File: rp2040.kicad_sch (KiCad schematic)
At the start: 10 parts, among them U1 RP2040, Y1 12 MHz

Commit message: Fixing buttons / Transitioning to new computer.
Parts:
- RST1: footprint ScottoKeebs_Components:Button_MJTP1243 -> 3rd_party_footprints:SW4_PTS815 SJM 250 SMTR LFS_CNK
- renumbered C1 to C10, C3 to C11, C6 to C12, C8 to C7, C7 to C8, C2 to C9, U1 to U3
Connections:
- no-connect marks 4 -> 24
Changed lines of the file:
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@@
+	)
+	(no_connect
+		(at 105.41 119.38)
+	)
+	(no_connect
+		(at 105.41 93.98)
 	)
 	(no_connect
@@
 	)
 	(no_connect
+		(at 105.41 124.46)
+	)
+	(no_connect
+		(at 105.41 101.6)
+	)
+	(no_connect
+		(at 105.41 91.44)
+	)
+	(no_connect
+		(at 105.41 127)
+	)
+	(no_connect
+		(at 105.41 137.16)
+	)
+	(no_connect
 		(at 69.85 58.42)
+	)
+	(no_connect
+		(at 105.41 121.92)
 	)
 	(no_connect
@@
 	(no_connect
 		(at 54.61 137.16)
+	)
+	(no_connect
+		(at 105.41 109.22)
+	)
+	(no_connect
+		(at 105.41 134.62)
+	)
+	(no_connect
+		(at 105.41 114.3)
+	)
+	(no_connect
+		(at 105.41 106.68)
+	)
+	(no_connect
+		(at 105.41 88.9)
+	)
+	(no_connect
+		(at 105.41 86.36)
+	)
+	(no_connect
+		(at 105.41 83.82)
+	)
+	(no_connect
+		(at 105.41 111.76)
+	)
+	(no_connect
+		(at 105.41 99.06)
+	)
+	(no_connect
+		(at 105.41 96.52)
+	)
+	(no_connect
+		(at 105.41 116.84)
+	)
+	(no_connect
+		(at 105.41 104.14)
 	)
 	(wire
@@
 		(in_pos_files yes)
 		(dnp no)
-		(property "Reference" "C3"
+		(property "Reference" "C11"
 			(at 86.868 49.784 90)
 			(show_name no)
@@
 			(project "steno"
 				(path "/238e1d3b-9ec5-448b-85c7-386a29cd2631/62364b54-274f-4b51-b5e4-9f0011b2e23c"
-					(reference "C3")
+					(reference "C11")
 					(unit 1)
 				)
@@
 		(dnp no)
 		(fields_autoplaced yes)
-		(property "Reference" "#PWR018"
+		(property "Reference" "#PWR017"
 			(at 27.94 118.11 0)
 			(hide yes)
@@
 			(project "steno"
 				(path "/238e1d3b-9ec5-448b-85c7-386a29cd2631/62364b54-274f-4b51-b5e4-9f0011b2e23c"
-					(reference "#PWR018")
+					(reference "#PWR017")
 					(unit 1)
 				)
@@
 		(dnp no)
 		(fields_autoplaced yes)
-		(property "Reference" "#PWR028"
+		(property "Reference" "#PWR018"
 			(at 30.48 78.74 0)
 			(hide yes)
@@
 			(project "steno"
 				(path "/238e1d3b-9ec5-448b-85c7-386a29cd2631/62364b54-274f-4b51-b5e4-9f0011b2e23c"
-					(reference "#PWR028")
+					(reference "#PWR018")
 					(unit 1)
 				)
@@
 		(dnp no)
 		(fields_autoplaced yes)
-		(property "Reference" "#PWR01"
+		(property "Reference" "#PWR021"
 			(at 48.26 73.66 0)
 			(hide yes)
@@
 			(project "steno"
 				(path "/238e1d3b-9ec5-448b-85c7-386a29cd2631/62364b54-274f-4b51-b5e4-9f0011b2e23c"
-					(reference "#PWR01")
+					(reference "#PWR021")
 					(unit 1)
 				)
@@
 		(in_pos_files yes)
 		(dnp no)
-		(property "Reference" "#PWR07"
+		(property "Reference" "#PWR024"
 			(at 69.85 59.69 0)
 			(hide yes)
@@
 			(project "steno"
 				(path "/238e1d3b-9ec5-448b-85c7-386a29cd2631/62364b54-274f-4b51-b5e4-9f0011b2e23c"
-					(reference "#PWR07")
+					(reference "#PWR024")
 					(unit 1)
 				)
@@
 		(in_pos_files yes)
 		(dnp no)
-		(property "Reference" "#PWR09"
+		(property "Reference" "#PWR028"
 			(at 90.17 52.07 0)
 			(hide yes)
@@
 			(project "steno"
 				(path "/238e1d3b-9ec5-448b-85c7-386a29cd2631/62364b54-274f-4b51-b5e4-9f0011b2e23c"
-					(reference "#PWR09")
+					(reference "#PWR028")
 					(unit 1)
 				)
@@
 		(dnp no)
 		(fields_autoplaced yes)
-		(property "Reference" "U1"
+		(property "Reference" "U3"
 			(at 82.1533 148.59 0)
 			(show_name no)
@@
 			(project "steno"
 				(path "/238e1d3b-9ec5-448b-85c7-386a29cd2631/62364b54-274f-4b51-b5e4-9f0011b2e23c"
-					(reference "U1")
+					(reference "U3")
 					(unit 1)
 				)
@@
 		(dnp no)
 		(fields_autoplaced yes)
-		(property "Reference" "#PWR04"
+		(property "Reference" "#PWR023"
 			(at 67.31 50.8 0)
 			(hide yes)
@@
 			(project "steno"
 				(path "/238e1d3b-9ec5-448b-85c7-386a29cd2631/62364b54-274f-4b51-b5e4-9f0011b2e23c"
-					(reference "#PWR04")
+					(reference "#PWR023")
 					(unit 1)
 				)
@@
 		(dnp no)
 		(fields_autoplaced yes)
-		(property "Reference" "#PWR02"
+		(property "Reference" "#PWR026"
 			(at 80.01 156.21 0)
 			(hide yes)
@@
 			(project "steno"
 				(path "/238e1d3b-9ec5-448b-85c7-386a29cd2631/62364b54-274f-4b51-b5e4-9f0011b2e23c"
-					(reference "#PWR02")
+					(reference "#PWR026")
 					(unit 1)
 				)
@@
 		(in_pos_files yes)
 		(dnp no)
-		(property "Reference" "#PWR06"
+		(property "Reference" "#PWR022"
 			(at 59.69 59.69 0)
 			(hide yes)
@@
 			(project "steno"
 				(path "/238e1d3b-9ec5-448b-85c7-386a29cd2631/62364b54-274f-4b51-b5e4-9f0011b2e23c"
-					(reference "#PWR06")
+					(reference "#PWR022")
 					(unit 1)
 				)
@@
 		(dnp no)
 		(fields_autoplaced yes)
-		(property "Reference" "C8"
+		(property "Reference" "C7"
 			(at 39.37 114.2999 0)
 			(show_name no)
@@
 			(project "steno"
 				(path "/238e1d3b-9ec5-448b-85c7-386a29cd2631/62364b54-274f-4b51-b5e4-9f0011b2e23c"
-					(reference "C8")
+					(reference "C7")
 					(unit 1)
 				)
@@
 		(dnp no)
 		(fields_autoplaced yes)
-		(property "Reference" "#PWR017"
+		(property "Reference" "#PWR019"
 			(at 35.56 143.51 0)
 			(hide yes)
@@
 			(project "steno"
 				(path "/238e1d3b-9ec5-448b-85c7-386a29cd2631/62364b54-274f-4b51-b5e4-9f0011b2e23c"
-					(reference "#PWR017")
+					(reference "#PWR019")
 					(unit 1)
 				)
@@
 		(dnp no)
 		(fields_autoplaced yes)
-		(property "Reference" "C7"
+		(property "Reference" "C8"
 			(at 39.37 132.0799 0)
 			(show_name no)
@@
 			(project "steno"
 				(path "/238e1d3b-9ec5-448b-85c7-386a29cd2631/62364b54-274f-4b51-b5e4-9f0011b2e23c"
-					(reference "C7")
+					(reference "C8")
 					(unit 1)
 				)
@@
 		(in_pos_files yes)
 		(dnp no)
-		(property "Reference" "C1"
+		(property "Reference" "C10"
 			(at 73.152 49.022 90)
 			(show_name no)
@@
 			(project "steno"
 				(path "/238e1d3b-9ec5-448b-85c7-386a29cd2631/62364b54-274f-4b51-b5e4-9f0011b2e23c"
-					(reference "C1")
+					(reference "C10")
 					(unit 1)
 				)
@@
 		(dnp no)
 		(fields_autoplaced yes)
-		(property "Reference" "C2"
+		(property "Reference" "C9"
 			(at 63.5 45.72 90)
 			(show_name no)
@@
 			(project "steno"
 				(path "/238e1d3b-9ec5-448b-85c7-386a29cd2631/62364b54-274f-4b51-b5e4-9f0011b2e23c"
-					(reference "C2")
+					(reference "C9")
 					(unit 1)
 				)
@@
 			)
 		)
-		(property "Footprint" "ScottoKeebs_Components:Button_MJTP1243"
+		(property "Footprint" "3rd_party_footprints:SW4_PTS815 SJM 250 SMTR LFS_CNK"
 			(at 36.83 62.23 0)
 			(hide yes)
@@
 		(dnp no)
 		(fields_autoplaced yes)
-		(property "Reference" "#PWR029"
+		(property "Reference" "#PWR020"
 			(at 44.45 69.85 0)
 			(hide yes)
@@
 			(project "steno"
 				(path "/238e1d3b-9ec5-448b-85c7-386a29cd2631/62364b54-274f-4b51-b5e4-9f0011b2e23c"
-					(reference "#PWR029")
+					(reference "#PWR020")
 					(unit 1)
 				)
@@
 		(in_pos_files yes)
 		(dnp no)
-		(property "Reference" "#PWR05"
+		(property "Reference" "#PWR025"
 			(at 77.47 50.8 0)
 			(hide yes)
@@
 			(project "steno"
 				(path "/238e1d3b-9ec5-448b-85c7-386a29cd2631/62364b54-274f-4b51-b5e4-9f0011b2e23c"
-					(reference "#PWR05")
+					(reference "#PWR025")
 					(unit 1)
 				)
@@
 		(dnp no)
 		(fields_autoplaced yes)
-		(property "Reference" "#PWR016"
+		(property "Reference" "#PWR029"
 			(at 97.79 59.69 0)
 			(hide yes)
@@
 			(project "steno"
 				(path "/238e1d3b-9ec5-448b-85c7-386a29cd2631/62364b54-274f-4b51-b5e4-9f0011b2e23c"
-					(reference "#PWR016")
+					(reference "#PWR029")
 					(unit 1)
 				)
@@
 		(in_pos_files yes)
 		(dnp no)
-		(property "Reference" "C6"
+		(property "Reference" "C12"
 			(at 98.298 46.736 90)
 			(show_name no)
@@
 			(project "steno"
 				(path "/238e1d3b-9ec5-448b-85c7-386a29cd2631/62364b54-274f-4b51-b5e4-9f0011b2e23c"
-					(reference "C6")
+					(reference "C12")
 					(unit 1)
 				)
@@
 		(in_pos_files yes)
 		(dnp no)
-		(property "Reference" "#PWR08"
+		(property "Reference" "#PWR027"
 			(at 82.55 45.72 0)
 			(hide yes)
@@
 			(project "steno"
 				(path "/238e1d3b-9ec5-448b-85c7-386a29cd2631/62364b54-274f-4b51-b5e4-9f0011b2e23c"
-					(reference "#PWR08")
+					(reference "#PWR027")
 					(unit 1)
 				)

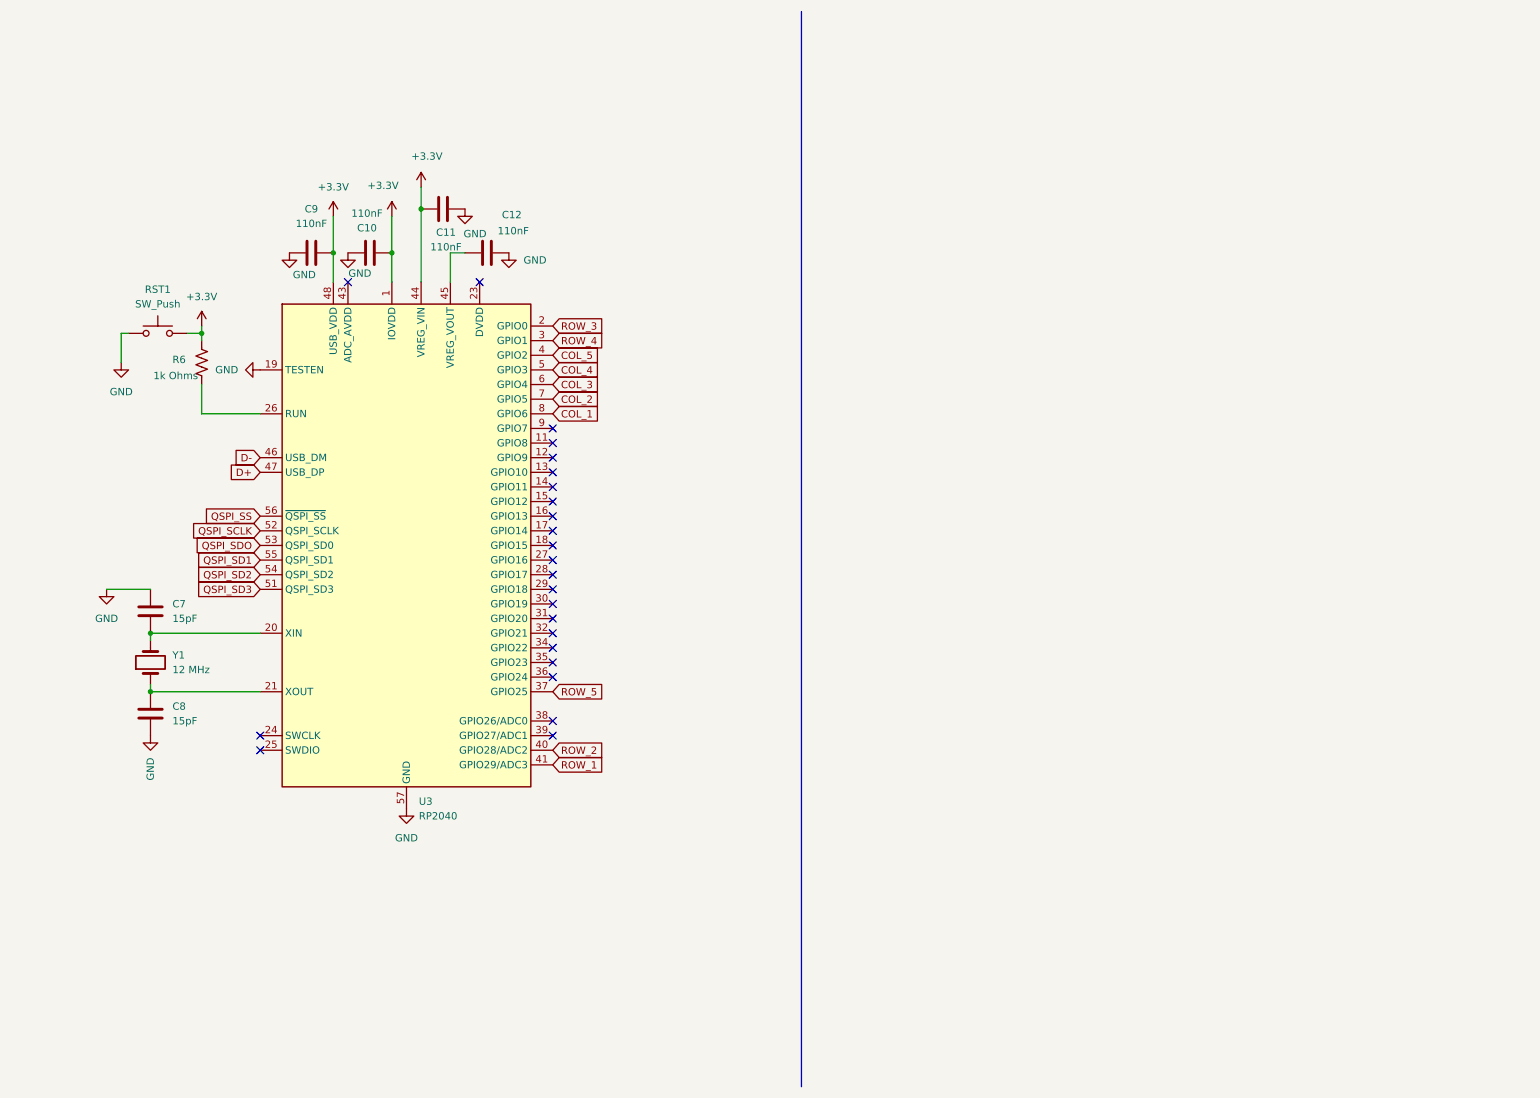
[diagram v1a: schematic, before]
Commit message: added status LED / Potential final changes
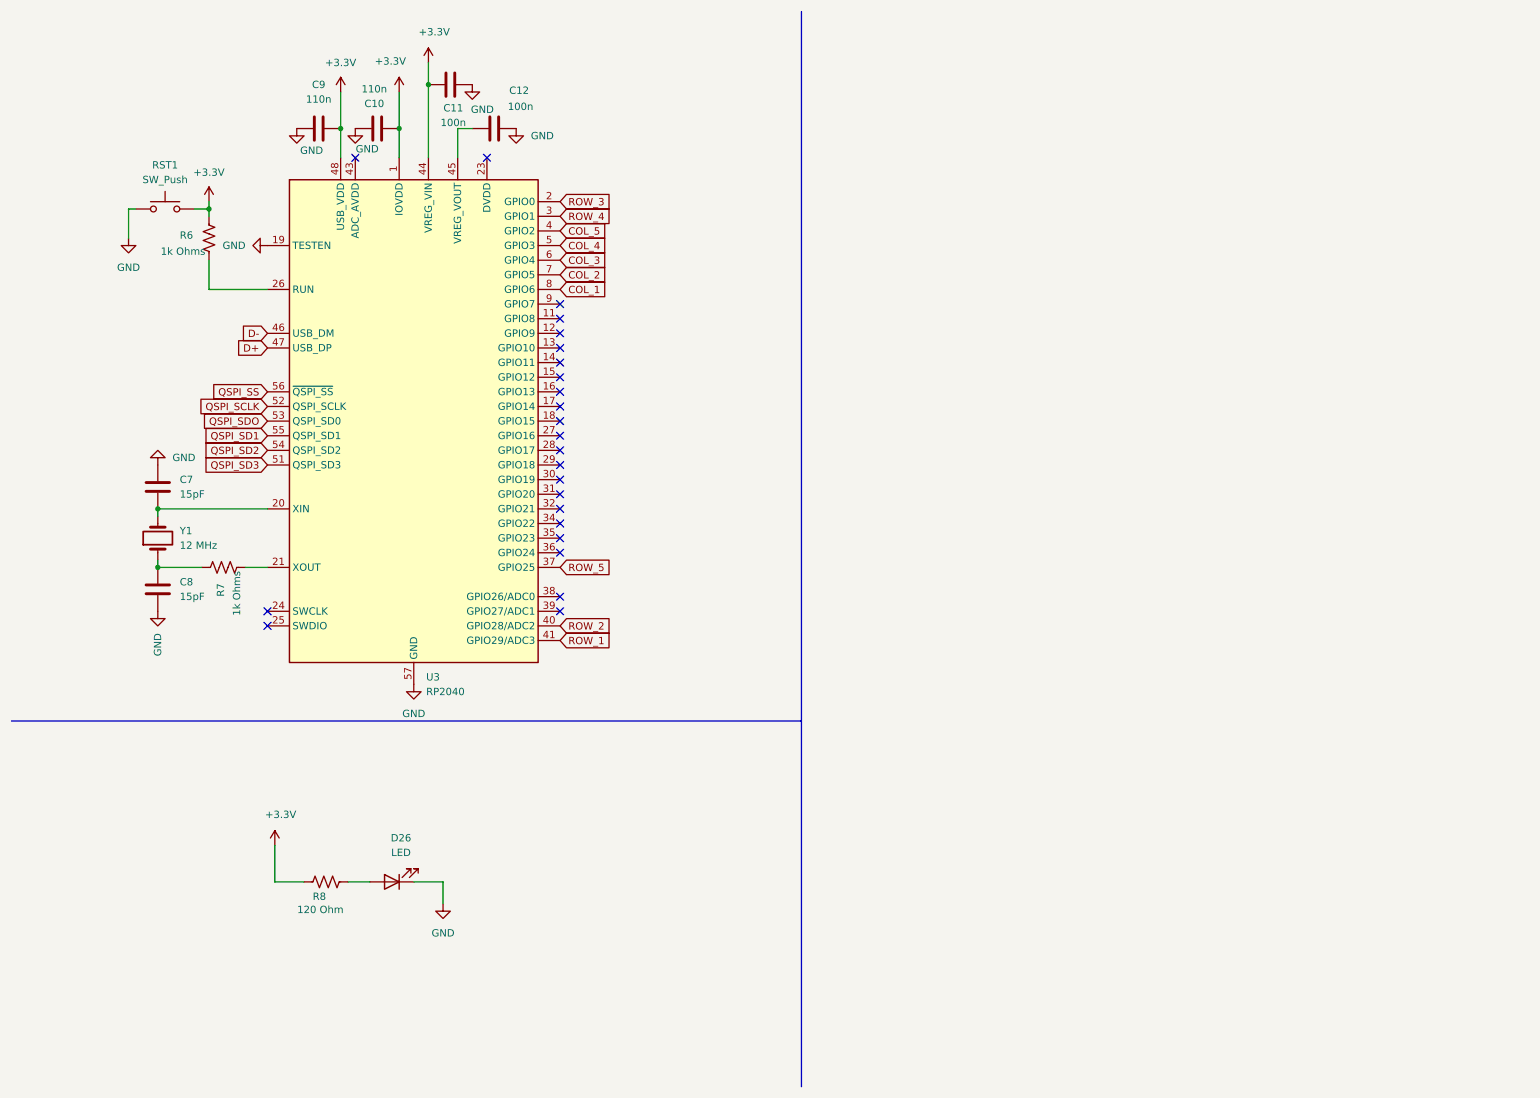
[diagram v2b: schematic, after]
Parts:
- added D26: LED, LED_SMD:LED_0201_0603Metric_Pad0.64x0.40mm_HandSolder, symbol Device:LED
- added R7: 1k Ohms, Resistor_SMD:R_0402_1005Metric_Pad0.72x0.64mm_HandSolder, symbol Device:R_US
- added R8: 120 Ohm, Resistor_SMD:R_0402_1005Metric_Pad0.72x0.64mm_HandSolder, symbol Device:R_US
- C10, C9: value 110nF -> 110n
- C11, C12: value 110nF -> 100n
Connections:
- net +3.3V: now also R8.1
- net GND: now also D26.1 (K)
- net at C8.1, Y1.1: now also R7.1; no longer U3.21 (XOUT)
- new net: D26.2 (A), R8.2
- new net: R7.2, U3.21 (XOUT)
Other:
- moved on the sheet: C10, C11, C12, C7, C8, C9, R6, RST1, U3, Y1

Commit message: Made changes based on feedback and RP2040 doc.
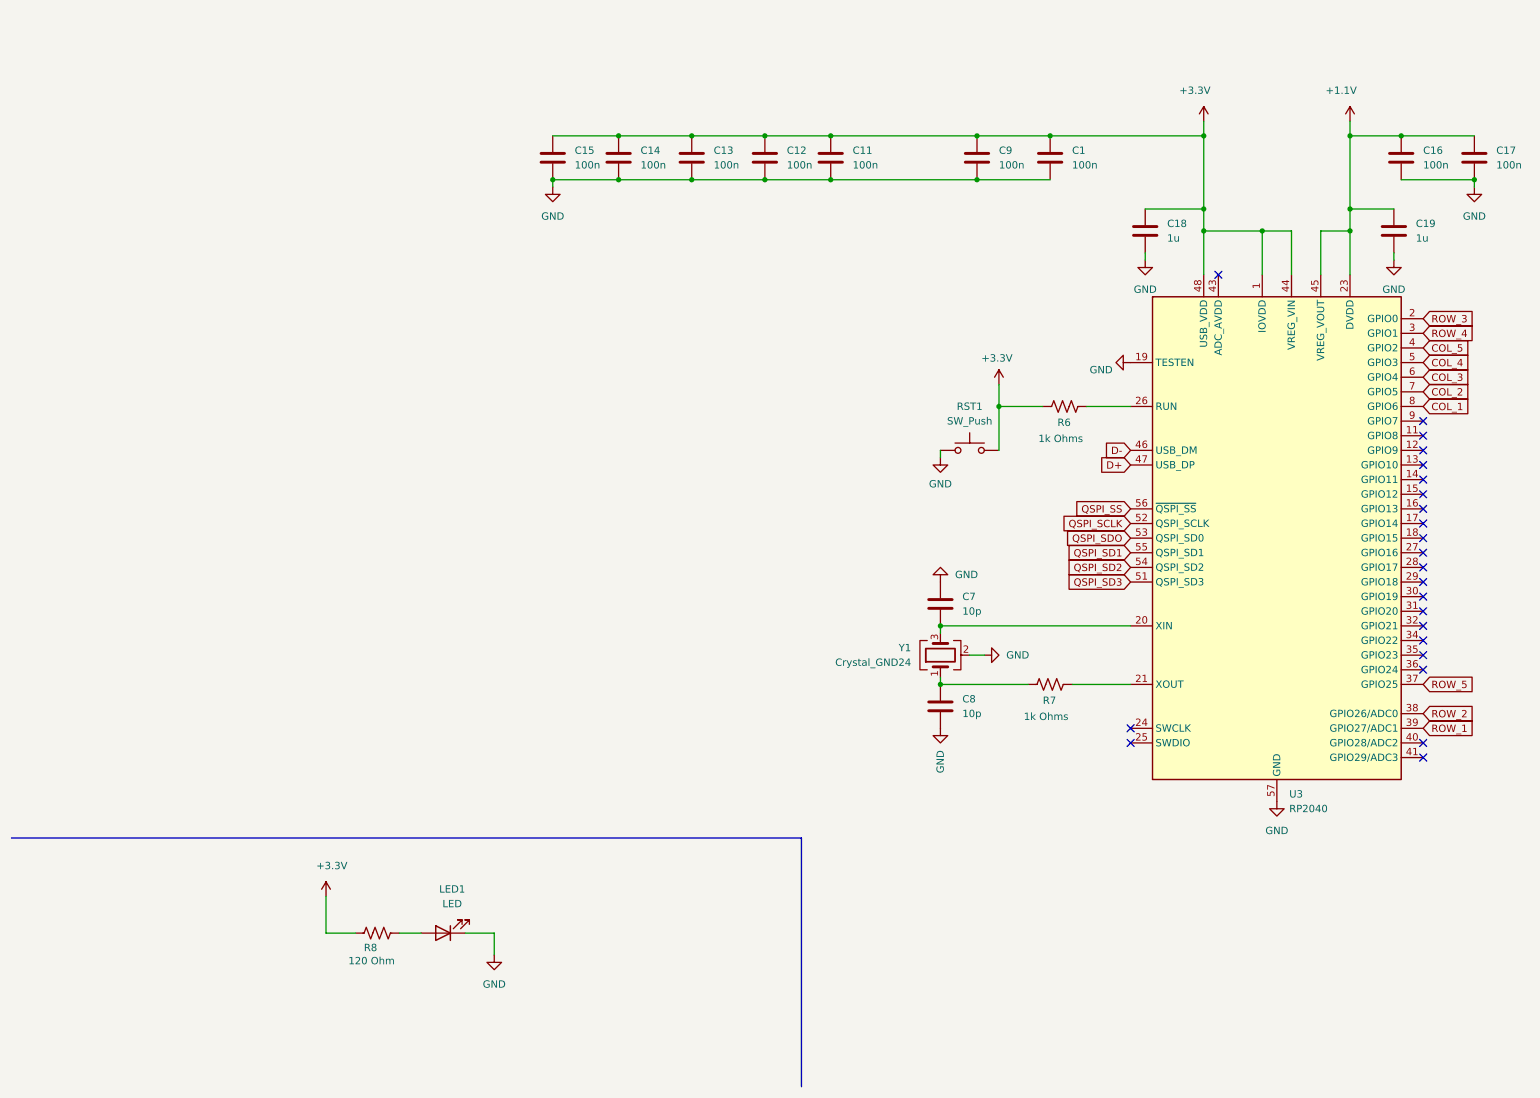
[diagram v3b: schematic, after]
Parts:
- removed C10: 110n, Capacitor_SMD:C_0402_1005Metric_Pad0.74x0.62mm_HandSolder, symbol Device:C
- removed Y1: 12 MHz, Crystal:Crystal_SMD_3215-2Pin_3.2x1.5mm, symbol Device:Crystal
- added C1, C13, C14, C15, C16, C17: 100n, Capacitor_SMD:C_0402_1005Metric, symbol Device:C
- added C18, C19: 1u, Capacitor_SMD:C_0402_1005Metric, symbol Device:C
- added Y1: Crystal_GND24, Crystal:Crystal_SMD_3225-4Pin_3.2x2.5mm_HandSoldering, symbol Device:Crystal_GND24
- C11, C12: footprint Capacitor_SMD:C_0402_1005Metric_Pad0.74x0.62mm_HandSolder -> Capacitor_SMD:C_0402_1005Metric
- C7, C8: value 15pF -> 10p; footprint Capacitor_SMD:C_0402_1005Metric_Pad0.74x0.62mm_HandSolder -> Capacitor_SMD:C_0402_1005Metric
- C9: value 110n -> 100n; footprint Capacitor_SMD:C_0402_1005Metric_Pad0.74x0.62mm_HandSolder -> Capacitor_SMD:C_0402_1005Metric
- LED1: renamed from D26; footprint LED_SMD:LED_0201_0603Metric_Pad0.64x0.40mm_HandSolder -> LED_SMD:LED_0402_1005Metric
- R6, R7, R8: footprint Resistor_SMD:R_0402_1005Metric_Pad0.72x0.64mm_HandSolder -> Resistor_SMD:R_0402_1005Metric
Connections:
- net +3.3V: now also C12.1, C1.1, C13.1, C14.1, C15.1, C18.1
- net GND: now also C1.2, C13.2, C14.2, C15.2, C16.2, C17.2, C18.2, C19.2, Y1.2 (G), Y1.4 (G)
- net ROW_1: now also U3.39 (GPIO27/ADC1); no longer U3.41 (GPIO29/ADC3)
- net ROW_2: now also U3.38 (GPIO26/ADC0); no longer U3.40 (GPIO28/ADC2)
- net at C7.1, U3.20 (XIN): now also Y1.3
- net +1.1V: now reaches U3.23 (DVDD), U3.50 (DVDD)
- net +1.1V: now also U3.45 (VREG_VOUT), C16.1, C17.1, C19.1
- net at C8.1, R7.1: now also Y1.1
- no-connect marks 24 -> 23
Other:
- moved on the sheet: C7, C8, LED1, R6, R7, R8, RST1, U3

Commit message: Savepoint!
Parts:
- C18, C19: footprint Capacitor_SMD:C_0402_1005Metric -> Capacitor_SMD:C_0603_1608Metric
- Y1: footprint Crystal:Crystal_SMD_3225-4Pin_3.2x2.5mm_HandSoldering -> Crystal:Crystal_SMD_3225-4Pin_3.2x2.5mm
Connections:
- net +3.3V: now also R6.2; no longer R6.1, RST1.2
- net at U3.26 (RUN): now also R6.1, RST1.2; no longer R6.2
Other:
- moved on the sheet: C1, C11, C12, C13, C14, C15, C9, R6, RST1

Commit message: Init Commit!
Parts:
- removed C1, C11, C12, C13, C14, C15, C16, C17, C9: 100n, Capacitor_SMD:C_0402_1005Metric, symbol Device:C
- removed C18, C19: 1u, Capacitor_SMD:C_0603_1608Metric, symbol Device:C
- removed C7, C8: 10p, Capacitor_SMD:C_0402_1005Metric, symbol Device:C
- removed LED1: LED, LED_SMD:LED_0402_1005Metric, symbol Device:LED
- removed R6, R7: 1k Ohms, Resistor_SMD:R_0402_1005Metric, symbol Device:R_US
- removed R8: 120 Ohm, Resistor_SMD:R_0402_1005Metric, symbol Device:R_US
- removed RST1: SW_Push, 3rd_party_footprints:SW4_PTS815 SJM 250 SMTR LFS_CNK, symbol Switch:SW_Push
- removed U3: RP2040, Package_DFN_QFN:QFN-56-1EP_7x7mm_P0.4mm_EP3.2x3.2mm, symbol MCU_RaspberryPi:RP2040
- removed Y1: Crystal_GND24, Crystal:Crystal_SMD_3225-4Pin_3.2x2.5mm, symbol Device:Crystal_GND24
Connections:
- no-connect marks 23 -> 0
